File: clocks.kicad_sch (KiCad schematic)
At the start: 8 parts, among them J7 CLKI_3TP, J8 SEL_3TP, J9 CLKO_3TP, U3 CDCE906PWR

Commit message: printed pdf from schematics
Signed-off-by: Mika Laitio <lamikr@gmail.com>
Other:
- company: (none) -> Mika Laitio
- title: (none) -> I2S Audio to AES/EBU Optical Toslink
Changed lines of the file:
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@@
   (paper "A4")
   (title_block
+    (title "I2S Audio to AES/EBU Optical Toslink")
     (date "2023-12-26")
     (rev "v0.1")
+    (company "Mika Laitio")
   )
   (junction (at 132.842 68.326) (diameter 0) (color 0 0 0 0)

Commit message: added mpn and sku_digikey numbers for bom
Signed-off-by: Mika Laitio <lamikr@gmail.com>
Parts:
- C13, C14, C15, C16: MFR (none) -> Murata; MPN (none) -> GRM033R61A104ME15D; SKU_DIGIKEY (none) -> 490-5405-1-ND
- U3: MFR (none) -> TI; MPN (none) -> CDCE906PWR; Price (none) -> 5.18; SKU_DIGIKEY (none) -> 296-26038-2-ND
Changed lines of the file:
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@@
+      (effects (font (size 1.27 1.27)) hide)
+    )
+    (property "Notes" "" (at 78.232 30.226 0)
+      (effects (font (size 1.27 1.27)) hide)
+    )
+    (property "Price" "" (at 78.232 30.226 0)
+      (effects (font (size 1.27 1.27)) hide)
+    )
+    (property "MFR" "Murata" (at 78.232 30.226 0)
+      (effects (font (size 1.27 1.27)) hide)
+    )
+    (property "MPN" "GRM033R61A104ME15D" (at 78.232 30.226 0)
+      (effects (font (size 1.27 1.27)) hide)
+    )
+    (property "SKU_DIGIKEY" "490-5405-1-ND " (at 78.232 30.226 0)
       (effects (font (size 1.27 1.27)) hide)
     )
@@
       (effects (font (size 1.27 1.27)) hide)
     )
+    (property "Notes" "" (at 43.942 30.226 0)
+      (effects (font (size 1.27 1.27)) hide)
+    )
+    (property "Price" "" (at 43.942 30.226 0)
+      (effects (font (size 1.27 1.27)) hide)
+    )
+    (property "MFR" "Murata" (at 43.942 30.226 0)
+      (effects (font (size 1.27 1.27)) hide)
+    )
+    (property "MPN" "GRM033R61A104ME15D" (at 43.942 30.226 0)
+      (effects (font (size 1.27 1.27)) hide)
+    )
+    (property "SKU_DIGIKEY" "490-5405-1-ND " (at 43.942 30.226 0)
+      (effects (font (size 1.27 1.27)) hide)
+    )
     (pin "1")
     (pin "2")
@@
       (effects (font (size 1.27 1.27)) hide)
     )
+    (property "Notes" "" (at 56.642 30.226 0)
+      (effects (font (size 1.27 1.27)) hide)
+    )
+    (property "Price" "" (at 56.642 30.226 0)
+      (effects (font (size 1.27 1.27)) hide)
+    )
+    (property "MFR" "Murata" (at 56.642 30.226 0)
+      (effects (font (size 1.27 1.27)) hide)
+    )
+    (property "MPN" "GRM033R61A104ME15D" (at 56.642 30.226 0)
+      (effects (font (size 1.27 1.27)) hide)
+    )
+    (property "SKU_DIGIKEY" "490-5405-1-ND " (at 56.642 30.226 0)
+      (effects (font (size 1.27 1.27)) hide)
+    )
     (pin "1")
     (pin "2")
@@
     )
     (property "Datasheet" "~" (at 151.892 54.356 0)
+      (effects (font (size 1.27 1.27)) hide)
+    )
+    (property "Notes" "" (at 151.892 54.356 0)
+      (effects (font (size 1.27 1.27)) hide)
+    )
+    (property "Price" "" (at 151.892 54.356 0)
       (effects (font (size 1.27 1.27)) hide)
     )
@@
       (effects (font (size 1.27 1.27) italic) hide)
     )
-    (property "Datasheet" "CDCE906PWR" (at 82.042 40.386 0)
+    (property "Datasheet" "~" (at 82.042 40.386 0)
       (effects (font (size 1.27 1.27) italic) hide)
+    )
+    (property "Notes" "" (at 82.042 40.386 0)
+      (effects (font (size 1.27 1.27)) hide)
+    )
+    (property "Price" "5.18" (at 82.042 40.386 0)
+      (effects (font (size 1.27 1.27)) hide)
+    )
+    (property "MFR" "TI" (at 82.042 40.386 0)
+      (effects (font (size 1.27 1.27)) hide)
+    )
+    (property "MPN" "CDCE906PWR" (at 82.042 40.386 0)
+      (effects (font (size 1.27 1.27)) hide)
+    )
+    (property "SKU_DIGIKEY" "296-26038-2-ND" (at 82.042 40.386 0)
+      (effects (font (size 1.27 1.27)) hide)
     )
     (pin "18")
@@
       (effects (font (size 1.27 1.27)) hide)
     )
+    (property "Notes" "" (at 68.072 30.226 0)
+      (effects (font (size 1.27 1.27)) hide)
+    )
+    (property "Price" "" (at 68.072 30.226 0)
+      (effects (font (size 1.27 1.27)) hide)
+    )
+    (property "MFR" "Murata" (at 68.072 30.226 0)
+      (effects (font (size 1.27 1.27)) hide)
+    )
+    (property "MPN" "GRM033R61A104ME15D" (at 68.072 30.226 0)
+      (effects (font (size 1.27 1.27)) hide)
+    )
+    (property "SKU_DIGIKEY" "490-5405-1-ND " (at 68.072 30.226 0)
+      (effects (font (size 1.27 1.27)) hide)
+    )
     (pin "1")
     (pin "2")
@@
       (effects (font (size 1.27 1.27)) hide)
     )
+    (property "Notes" "" (at 49.022 68.326 0)
+      (effects (font (size 1.27 1.27)) hide)
+    )
+    (property "Price" "" (at 49.022 68.326 0)
+      (effects (font (size 1.27 1.27)) hide)
+    )
     (pin "3")
     (pin "2")
@@
       (effects (font (size 1.27 1.27)) hide)
     )
+    (property "Notes" "" (at 33.782 67.056 0)
+      (effects (font (size 1.27 1.27)) hide)
+    )
+    (property "Price" "" (at 33.782 67.056 0)
+      (effects (font (size 1.27 1.27)) hide)
+    )

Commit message: optimized bom from digikey
Signed-off-by: Mika Laitio <lamikr@gmail.com>
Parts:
- C13, C14, C15, C16: QtyOrdered (none) -> 100
- U3: QtyOrdered (none) -> 3; SKU_DIGIKEY 296-26038-2-ND -> 296-26038-1-ND
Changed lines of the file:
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@@
+      (effects (font (size 1.27 1.27)) hide)
+    )
+    (property "QtyOrdered" "100" (at 78.232 30.226 0)
       (effects (font (size 1.27 1.27)) hide)
     )
@@
       (effects (font (size 1.27 1.27)) hide)
     )
+    (property "QtyOrdered" "100" (at 43.942 30.226 0)
+      (effects (font (size 1.27 1.27)) hide)
+    )
     (pin "1")
     (pin "2")
@@
       (effects (font (size 1.27 1.27)) hide)
     )
+    (property "QtyOrdered" "100" (at 56.642 30.226 0)
+      (effects (font (size 1.27 1.27)) hide)
+    )
     (pin "1")
     (pin "2")
@@
     )
     (property "Price" "" (at 151.892 54.356 0)
+      (effects (font (size 1.27 1.27)) hide)
+    )
+    (property "QtyOrdered" "" (at 151.892 54.356 0)
       (effects (font (size 1.27 1.27)) hide)
     )
@@
       (effects (font (size 1.27 1.27)) hide)
     )
-    (property "SKU_DIGIKEY" "296-26038-2-ND" (at 82.042 40.386 0)
+    (property "SKU_DIGIKEY" "296-26038-1-ND" (at 82.042 40.386 0)
+      (effects (font (size 1.27 1.27)) hide)
+    )
+    (property "QtyOrdered" "3" (at 82.042 40.386 0)
       (effects (font (size 1.27 1.27)) hide)
     )
@@
       (effects (font (size 1.27 1.27)) hide)
     )
+    (property "QtyOrdered" "100" (at 68.072 30.226 0)
+      (effects (font (size 1.27 1.27)) hide)
+    )
     (pin "1")
     (pin "2")
@@
       (effects (font (size 1.27 1.27)) hide)
     )
+    (property "QtyOrdered" "" (at 49.022 68.326 0)
+      (effects (font (size 1.27 1.27)) hide)
+    )
     (pin "3")
     (pin "2")
@@
       (effects (font (size 1.27 1.27)) hide)
     )
+    (property "QtyOrdered" "" (at 33.782 67.056 0)
+      (effects (font (size 1.27 1.27)) hide)
+    )

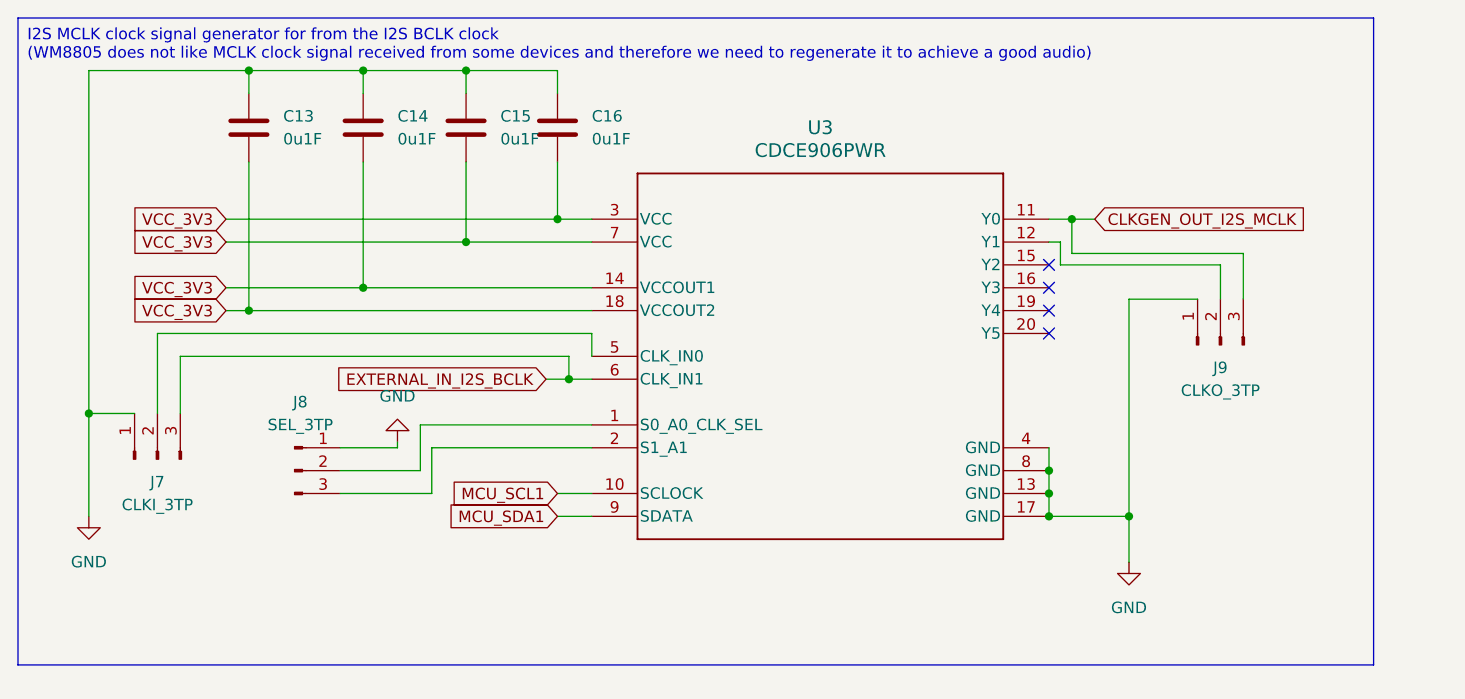
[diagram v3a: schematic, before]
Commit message: various updates
- removed duplicates 5V power connectors
- now the whole pcb is always powered via 6 pin
  atmega avr isp connector
- added connector for wm8805 rx0 and rx1
- added labels for jumpers/connectors
- moved the orientation of existing connecors
- moved the location of ldo close to
  6 pin avr isp connector

Signed-off-by: Mika Laitio <lamikr@gmail.com>
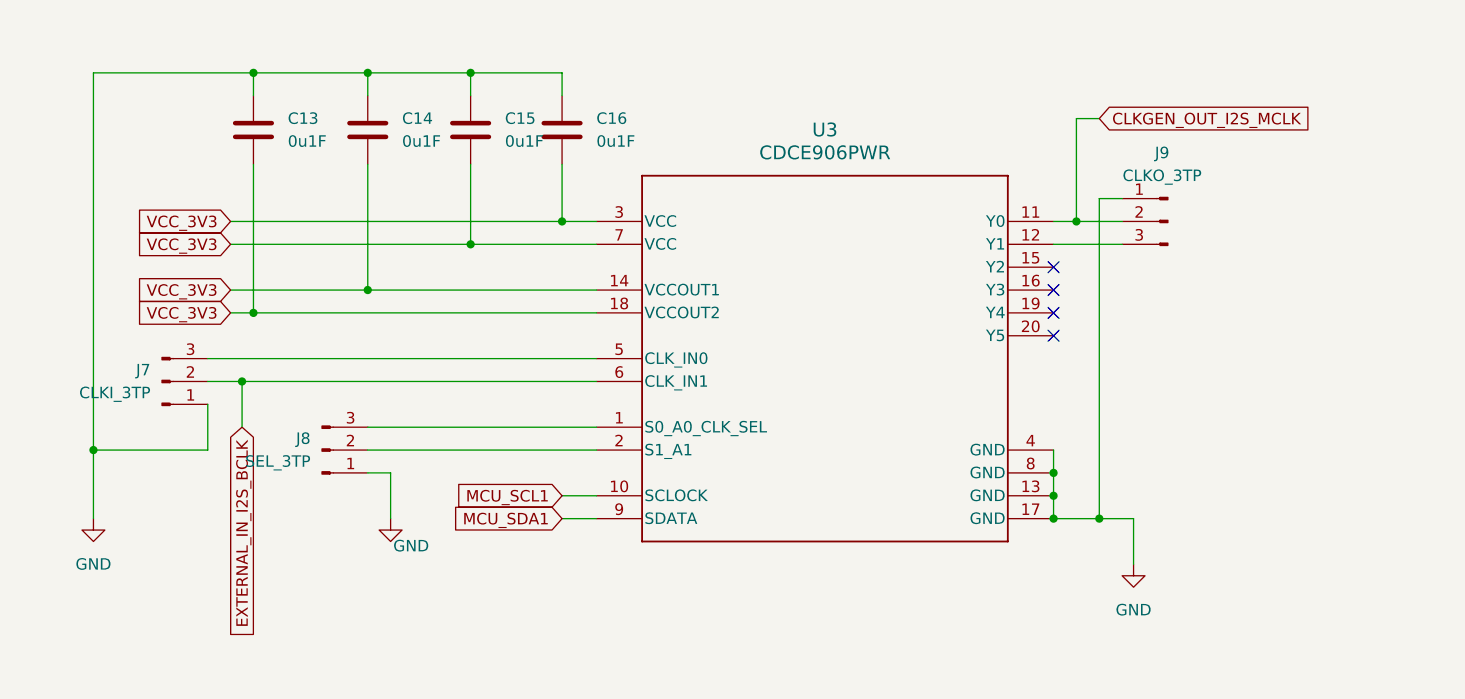
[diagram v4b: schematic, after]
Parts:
- J7, J8, J9: footprint Connector_PinHeader_1.27mm:PinHeader_1x03_P1.27mm_Vertical -> Connector_PinHeader_2.54mm:PinHeader_1x03_P2.54mm_Vertical
- U3: footprint PW0020A-IPC_A -> lamikr_audio:PW0020A-IPC_A
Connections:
- net CLKGEN_OUT_I2S_MCLK: now also J9.2 (Pin_2); no longer J9.3 (Pin_3)
- net EXTERNAL_IN_I2S_BCLK: now also J7.2 (Pin_2); no longer J7.3 (Pin_3)
- net at U3.12 (Y1): now also J9.3 (Pin_3); no longer J9.2 (Pin_2)
- net at U3.1 (S0_A0_CLK_SEL): now also J8.3 (Pin_3); no longer J8.2 (Pin_2)
- net at U3.2 (S1_A1): now also J8.2 (Pin_2); no longer J8.3 (Pin_3)
- net at U3.5 (CLK_IN0): now also J7.3 (Pin_3); no longer J7.2 (Pin_2)
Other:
- moved on the sheet: C13, C14, C15, C16, J7, J8, J9, U3

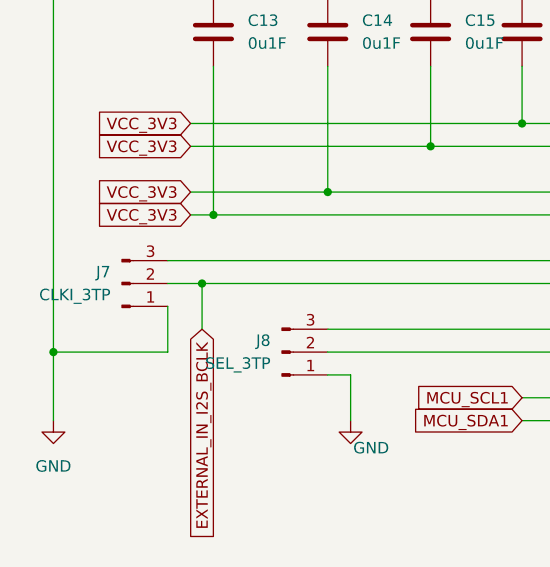
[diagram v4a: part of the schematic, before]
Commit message: finished v0.2 design
- mcu ftdi serial connector reset pin
  to 3v3 instead of 5v
- 3.3v pull-up resistor, cap and diode for mcu reset
- mcu reset button
- solder paste clearance -20% for
  mcu, codec, clk gen and ldo to help
  spreading pasta to small pins close to
  ech others

Signed-off-by: Mika Laitio <lamikr@gmail.com>
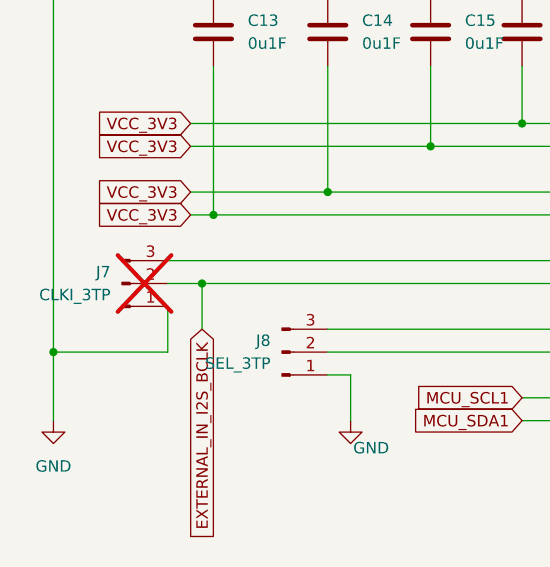
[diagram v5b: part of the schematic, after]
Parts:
- J7: now not fitted
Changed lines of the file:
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@@
 	(title_block
 		(title "I2S Audio to AES/EBU Optical Toslink")
-		(date "2023-12-26")
-		(rev "v0.1")
+		(date "2024-03-18")
+		(rev "v0.2")
 		(company "Mika Laitio")
 	)
@@
 		(in_bom yes)
 		(on_board yes)
-		(dnp no)
+		(dnp yes)
 		(property "Reference" "J7"
 			(at 33.02 57.1499 0)

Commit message: component footprint updates
- 0402 caps and resistors to 0603
- reset pin-header to reset button

Signed-off-by: Mika Laitio <lamikr@gmail.com>
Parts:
- C13, C14, C15, C16: footprint Capacitor_SMD:C_0402_1005Metric -> Capacitor_SMD:C_0603_1608Metric
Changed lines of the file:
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@@
 			)
 		)
-		(property "Footprint" "Capacitor_SMD:C_0402_1005Metric"
+		(property "Footprint" "Capacitor_SMD:C_0603_1608Metric"
 			(at 79.7052 34.29 0)
 			(effects
@@
 			)
 		)
-		(property "Footprint" "Capacitor_SMD:C_0402_1005Metric"
+		(property "Footprint" "Capacitor_SMD:C_0603_1608Metric"
 			(at 45.4152 34.29 0)
 			(effects
@@
 			)
 		)
-		(property "Footprint" "Capacitor_SMD:C_0402_1005Metric"
+		(property "Footprint" "Capacitor_SMD:C_0603_1608Metric"
 			(at 58.1152 34.29 0)
 			(effects
@@
 			)
 		)
-		(property "Footprint" "Capacitor_SMD:C_0402_1005Metric"
+		(property "Footprint" "Capacitor_SMD:C_0603_1608Metric"
 			(at 69.5452 34.29 0)
 			(effects
